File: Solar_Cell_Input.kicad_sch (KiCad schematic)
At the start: 41 parts, among them J2701 PT_1000, Q201 NMOS, Q202 NMOS, Q203 NMOS, Q204 NMOS, U201 BQ24650

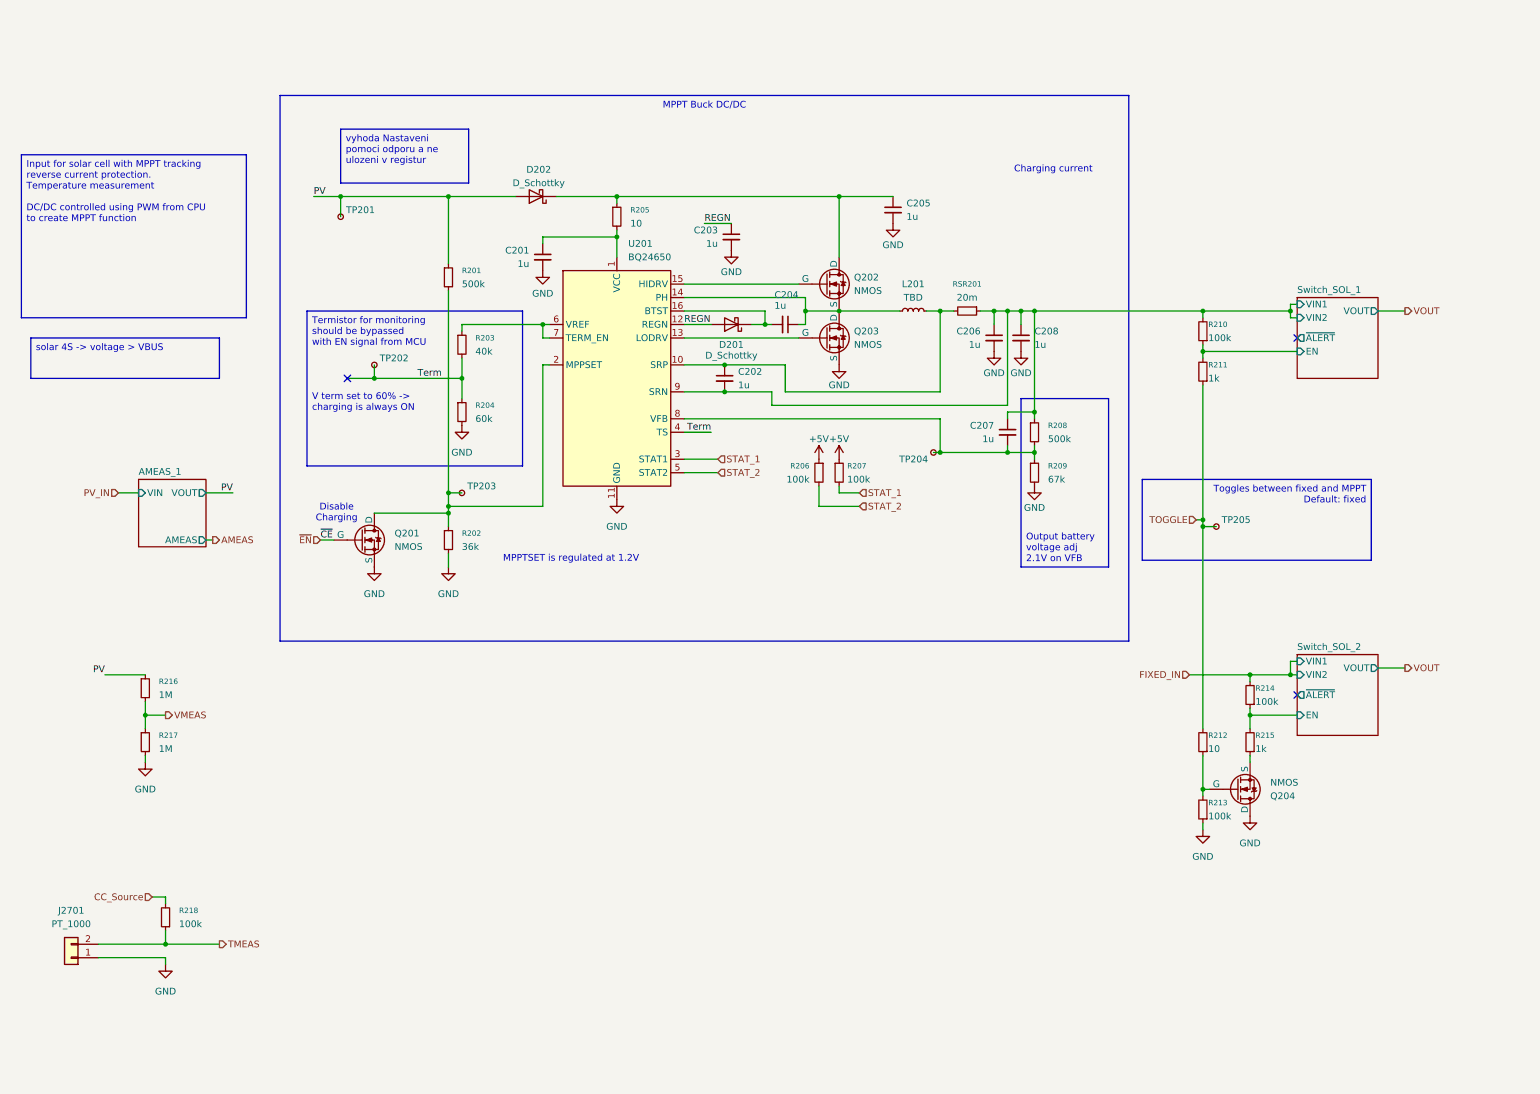
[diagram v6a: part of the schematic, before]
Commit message: restructurization of the entire project improved
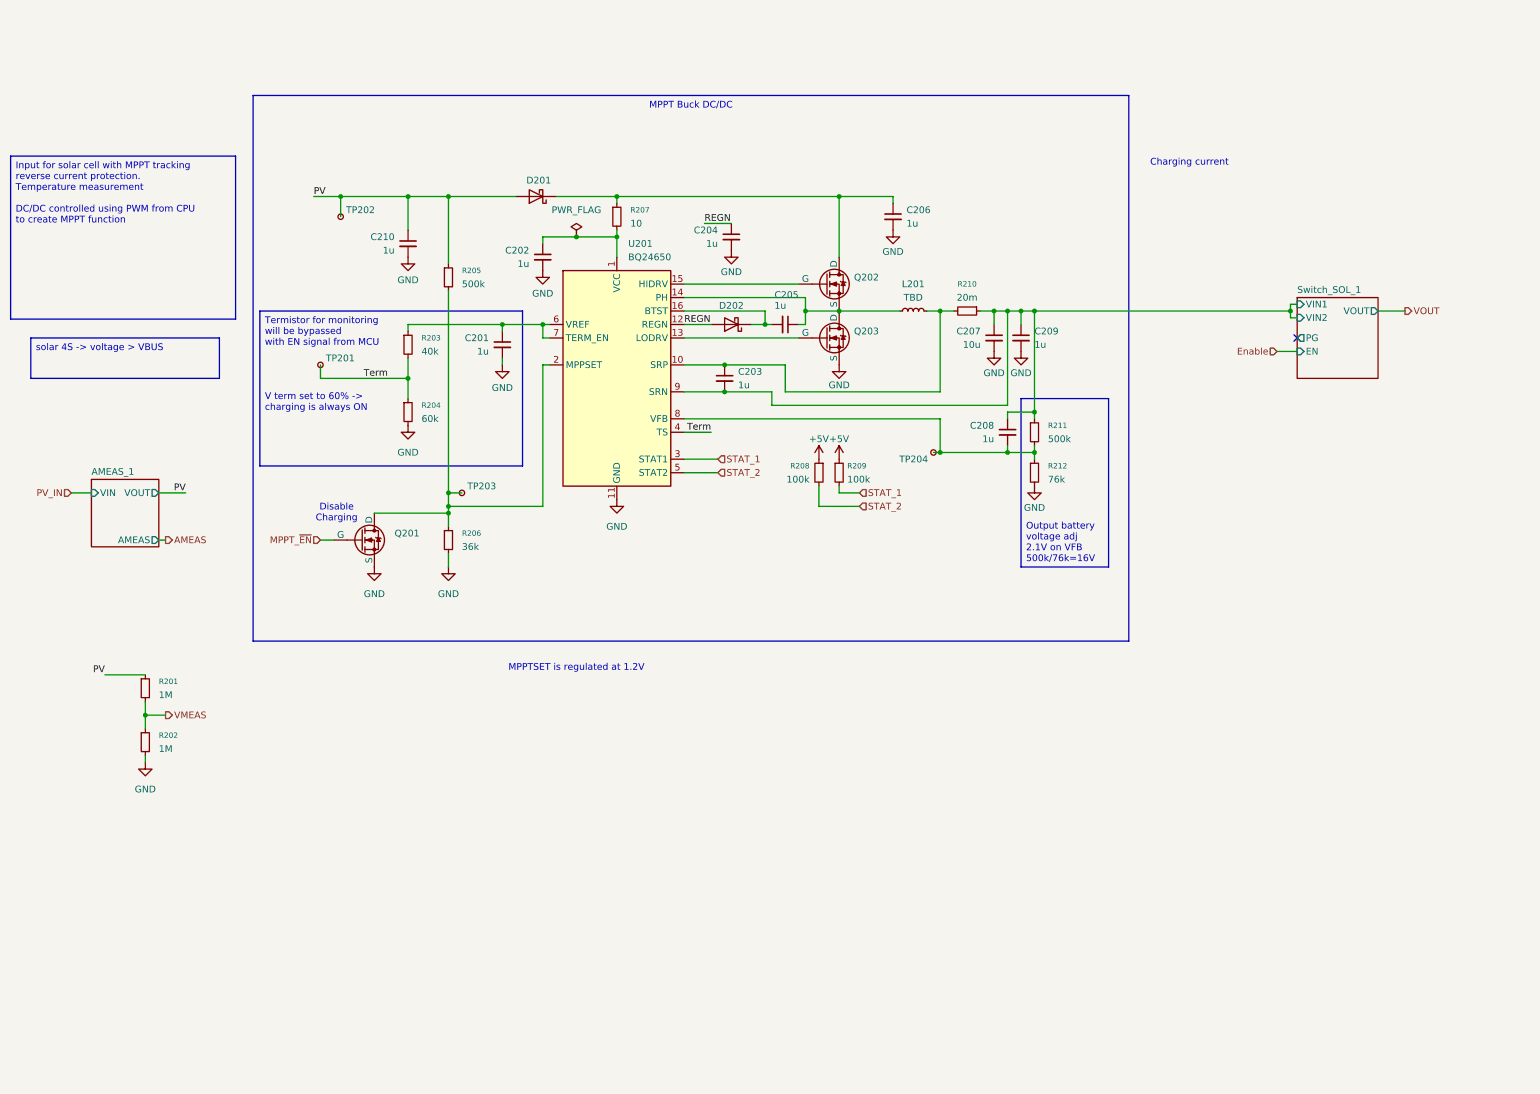
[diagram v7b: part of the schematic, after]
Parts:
- removed J2701: PT_1000, Connector_PinSocket_2.54mm:PinSocket_1x02_P2.54mm_Vertical, symbol Connector_Generic:Conn_01x02
- removed Q204: NMOS, Package_TO_SOT_SMD:SOT-23-3, symbol Simulation_SPICE:NMOS
- removed R210, R213, R214, R218: 100k, Resistor_SMD:R_0603_1608Metric_Pad0.98x0.95mm_HandSolder, symbol Device:R_Small
- removed R211, R215: 1k, Resistor_SMD:R_0603_1608Metric_Pad0.98x0.95mm_HandSolder, symbol Device:R_Small
- removed R212: 10, Resistor_SMD:R_0603_1608Metric_Pad0.98x0.95mm_HandSolder, symbol Device:R_Small
- removed TP205: ~, TestPoint:TestPoint_Pad_1.0x1.0mm, symbol Connector:TestPoint_Small
- added C201, C210: 1u, Capacitor_SMD:C_0603_1608Metric_Pad1.08x0.95mm_HandSolder, symbol Device:C_Small
- C207: renamed from C206; value 1u -> 10u
- Q201: value NMOS -> IRLML5103
- Q202, Q203: value NMOS -> NVTFWS4D9N04XMTAG
- R212: renamed from R209; value 67k -> 76k
- renumbered C201 to C202, C202 to C203, C203 to C204, C204 to C205, C205 to C206, C207 to C208, C208 to C209, D202 to D201, D201 to D202, R216 to R201, R217 to R202, R201 to R205, R202 to R206, R205 to R207, R206 to R208, R207 to R209, RSR201 to R210, R208 to R211, TP202 to TP201, TP201 to TP202
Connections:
- net GND: now also C201.2, C210.2
- net PV: now also C210.1
- net at R203.1, U201.6 (VREF), U201.7 (TERM_EN): now also C201.1
- net ~{EN} renamed MPPT_~{EN}
- no-connect marks 3 -> 1
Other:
- removed sheet Switch_SOL_2
- sheet Switch_SOL_1 ports: added PG; removed ~{ALERT}
- moved on the sheet: C206, R203, R204, TP201

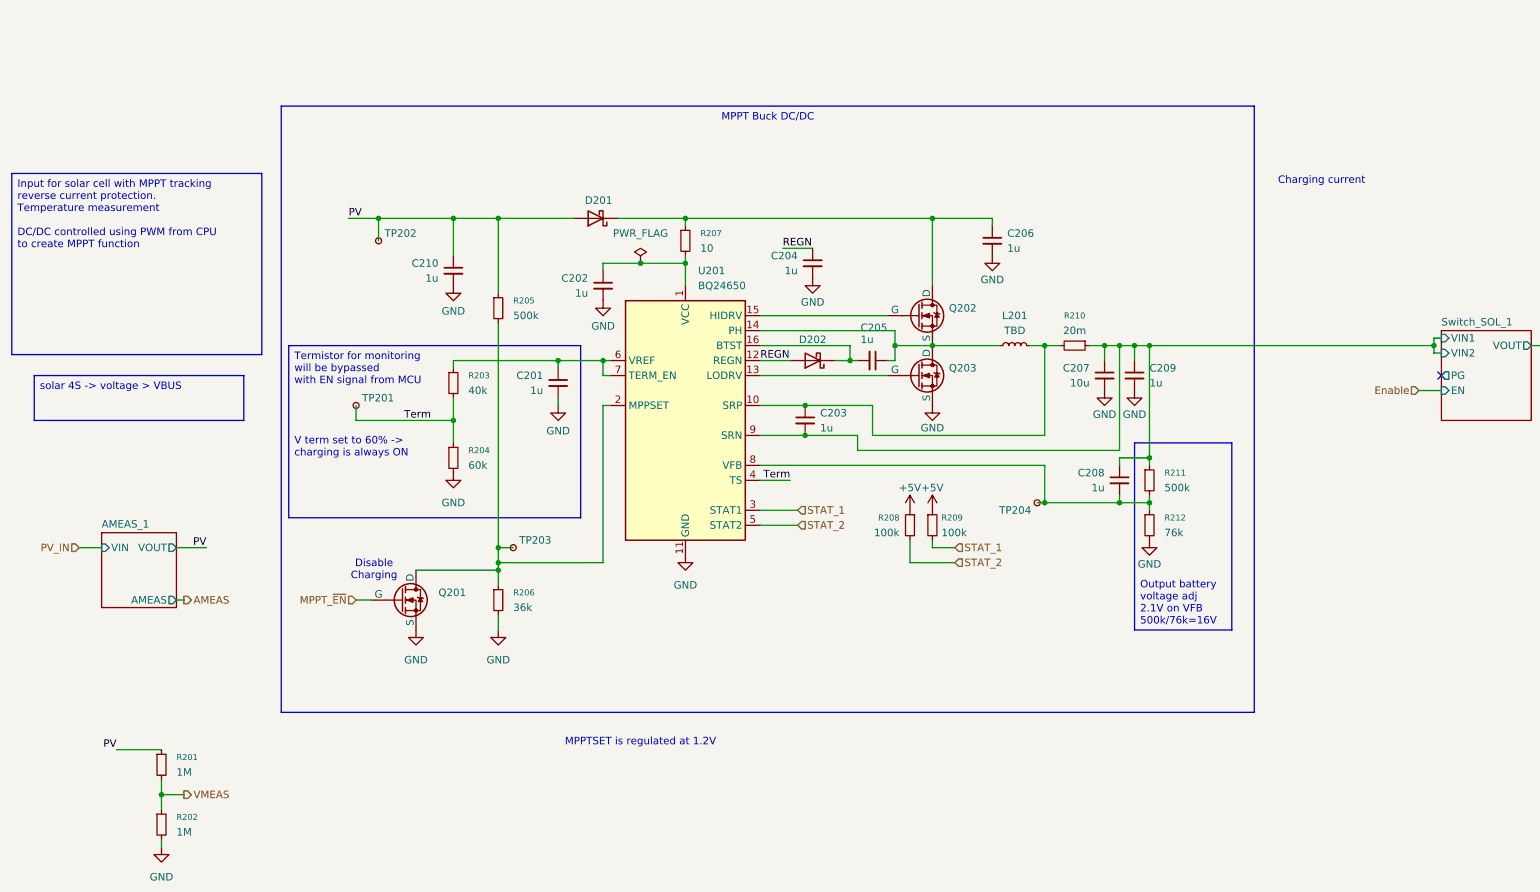
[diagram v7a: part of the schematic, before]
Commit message: added universal switch, added simples current source, reworked test schematic and pcb
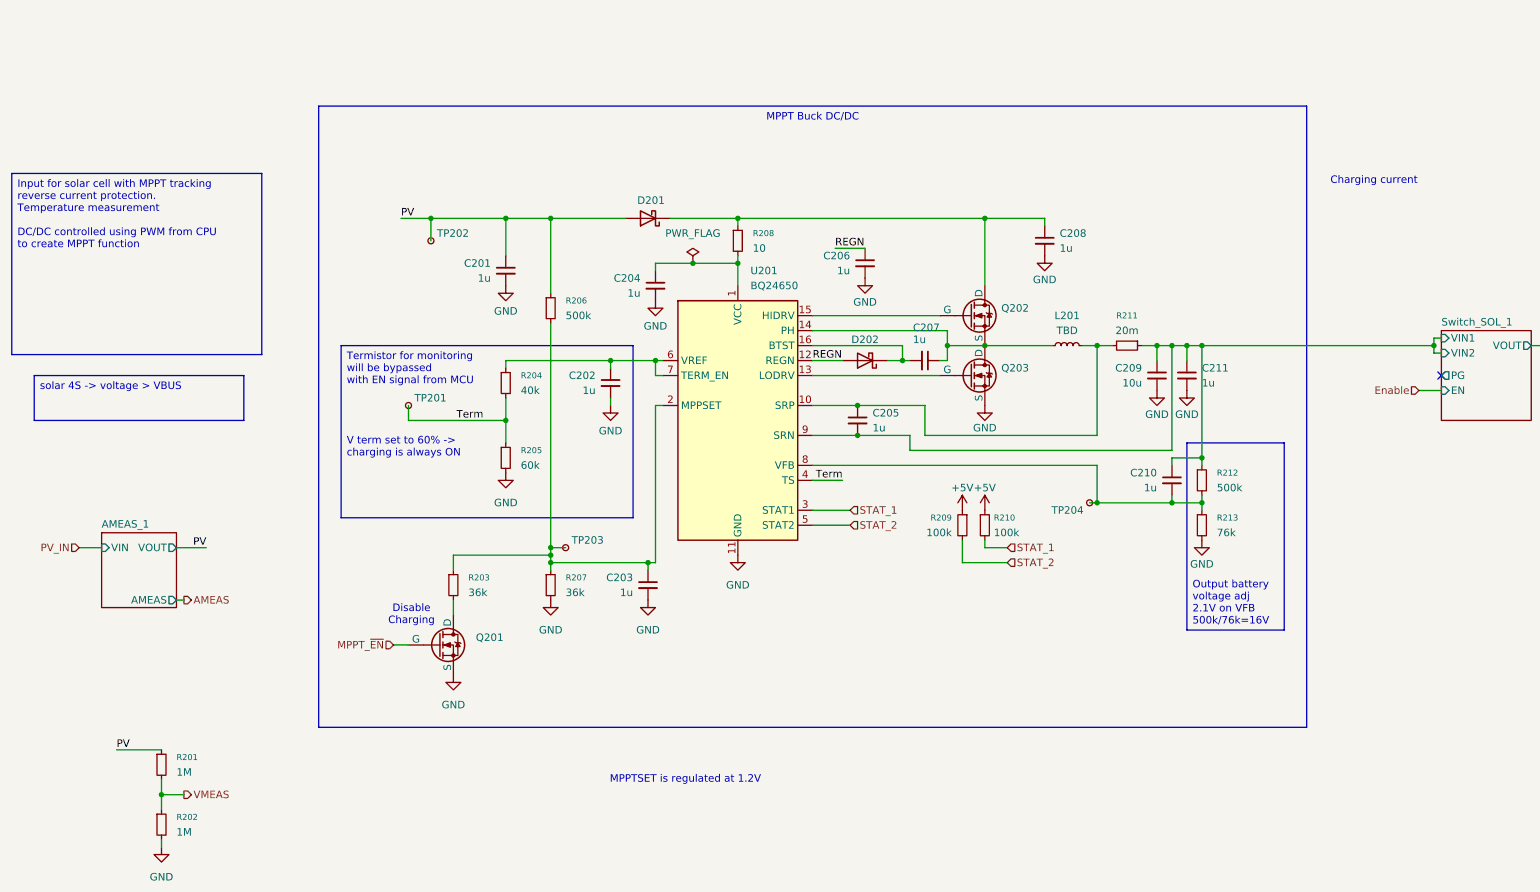
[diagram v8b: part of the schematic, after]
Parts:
- added C203: 1u, Capacitor_SMD:C_0603_1608Metric_Pad1.08x0.95mm_HandSolder, symbol Device:C_Small
- added R203: 36k, Resistor_SMD:R_0603_1608Metric_Pad0.98x0.95mm_HandSolder, symbol Device:R_Small
- renumbered C210 to C201, C201 to C202, C202 to C204, C203 to C205, C204 to C206, C205 to C207, C206 to C208, C207 to C209, C208 to C210, C209 to C211, R203 to R204, R204 to R205, R205 to R206, R206 to R207, R207 to R208, R208 to R209, R209 to R210, R210 to R211, R211 to R212, R212 to R213
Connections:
- net GND: now also C203.2
- net at R206.2, R207.1, TP203.1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: now also C203.1, R203.1; no longer Q201.1 (D)
- new net: Q201.1 (D), R203.2
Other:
- moved on the sheet: C201, C202, C204, C205, C206, C207, C208, C209, C210, C211, D201, D202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
